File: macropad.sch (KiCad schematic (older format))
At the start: 13 parts

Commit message: added some wires
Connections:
- net labels added: COL0, COL1, GND, ROW0, ROW1, ROW2
- wire segments 0 -> 18
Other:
- moved on the sheet: D?, SW?
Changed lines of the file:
@@
 L Device:Rotary_Encoder_Switch SW?
 U 1 1 5D79E7D6
-P 3600 4300
-F 0 "SW?" H 3600 4667 50  0000 C CNN
-F 1 "Rotary_Encoder_Switch" H 3600 4576 50  0000 C CNN
-F 2 "" H 3450 4460 50  0001 C CNN
-F 3 "~" H 3600 4560 50  0001 C CNN
-	1    3600 4300
+P 3600 4350
+F 0 "SW?" H 3600 4717 50  0000 C CNN
+F 1 "Rotary_Encoder_Switch" H 3600 4626 50  0000 C CNN
+F 2 "" H 3450 4510 50  0001 C CNN
+F 3 "~" H 3600 4610 50  0001 C CNN
+	1    3600 4350
 	1    0    0    -1
 $EndComp
@@
 L Device:D_ALT D?
 U 1 1 5D79F668
-P 3900 4550
-F 0 "D?" V 3946 4471 50  0000 R CNN
-F 1 "D_ALT" V 3855 4471 50  0000 R CNN
-F 2 "" H 3900 4550 50  0001 C CNN
-F 3 "~" H 3900 4550 50  0001 C CNN
-	1    3900 4550
+P 3900 4600
+F 0 "D?" V 3946 4521 50  0000 R CNN
+F 1 "D_ALT" V 3855 4521 50  0000 R CNN
+F 2 "" H 3900 4600 50  0001 C CNN
+F 3 "~" H 3900 4600 50  0001 C CNN
+	1    3900 4600
 	0    -1   -1   0
 $EndComp
@@
 	0    -1   -1   0
 $EndComp
+Wire Wire Line
+	3950 2100 4300 2100
+Wire Wire Line
+	4300 2100 4300 3100
+Wire Wire Line
+	4300 3100 3900 3100
+Wire Wire Line
+	3900 4250 4300 4250
+Wire Wire Line
+	4300 4250 4300 3100
+Connection ~ 4300 3100
+Wire Wire Line
+	4300 2100 4300 1600
+Connection ~ 4300 2100
+Text GLabel 4300 1550 1    50   Input ~ 0
+COL0
+Text GLabel 5900 1550 1    50   Input ~ 0
+COL1
+Wire Wire Line
+	5900 1550 5900 2100
+Wire Wire Line
+	5900 2100 5650 2100
+Wire Wire Line
+	5900 2100 5900 3100
+Wire Wire Line
+	5900 3100 5650 3100
+Connection ~ 5900 2100
+Wire Wire Line
+	5900 3100 5900 4250
+Wire Wire Line
+	5900 4250 5650 4250
+Connection ~ 5900 3100
+Wire Wire Line
+	5650 2600 3950 2600
+Connection ~ 3950 2600
+Wire Wire Line
+	3950 2600 2800 2600
+Wire Wire Line
+	5650 3600 3900 3600
+Connection ~ 3900 3600
+Wire Wire Line
+	3900 3600 2800 3600
+Wire Wire Line
+	5650 4750 3900 4750
+Connection ~ 3900 4750
+Wire Wire Line
+	3900 4750 2800 4750
+Text GLabel 2800 2600 0    50   Input ~ 0
+ROW0
+Text GLabel 2800 3600 0    50   Input ~ 0
+ROW1
+Text GLabel 2800 4750 0    50   Input ~ 0
+ROW2
+Text GLabel 3350 2200 0    50   Input ~ 0
+GND
+Text GLabel 3300 3200 0    50   Input ~ 0
+GND
+Text GLabel 3300 4350 0    50   Input ~ 0
+GND
+Text GLabel 5050 2200 0    50   Input ~ 0
+GND
+Text GLabel 5050 3200 0    50   Input ~ 0
+GND
+Text GLabel 5050 4350 0    50   Input ~ 0
+GND
+Text GLabel 7100 2200 0    50   Input ~ 0
+GND
+Text GLabel 7100 2600 0    50   Input ~ 0
+ROW0
+Text GLabel 7100 2700 0    50   Input ~ 0
+ROW1
+Text GLabel 7100 2800 0    50   Input ~ 0
+ROW2
+Text GLabel 7100 2900 0    50   Input ~ 0
+COL0
+Text GLabel 7100 3000 0    50   Input ~ 0
+COL1
 $EndSCHEMATC

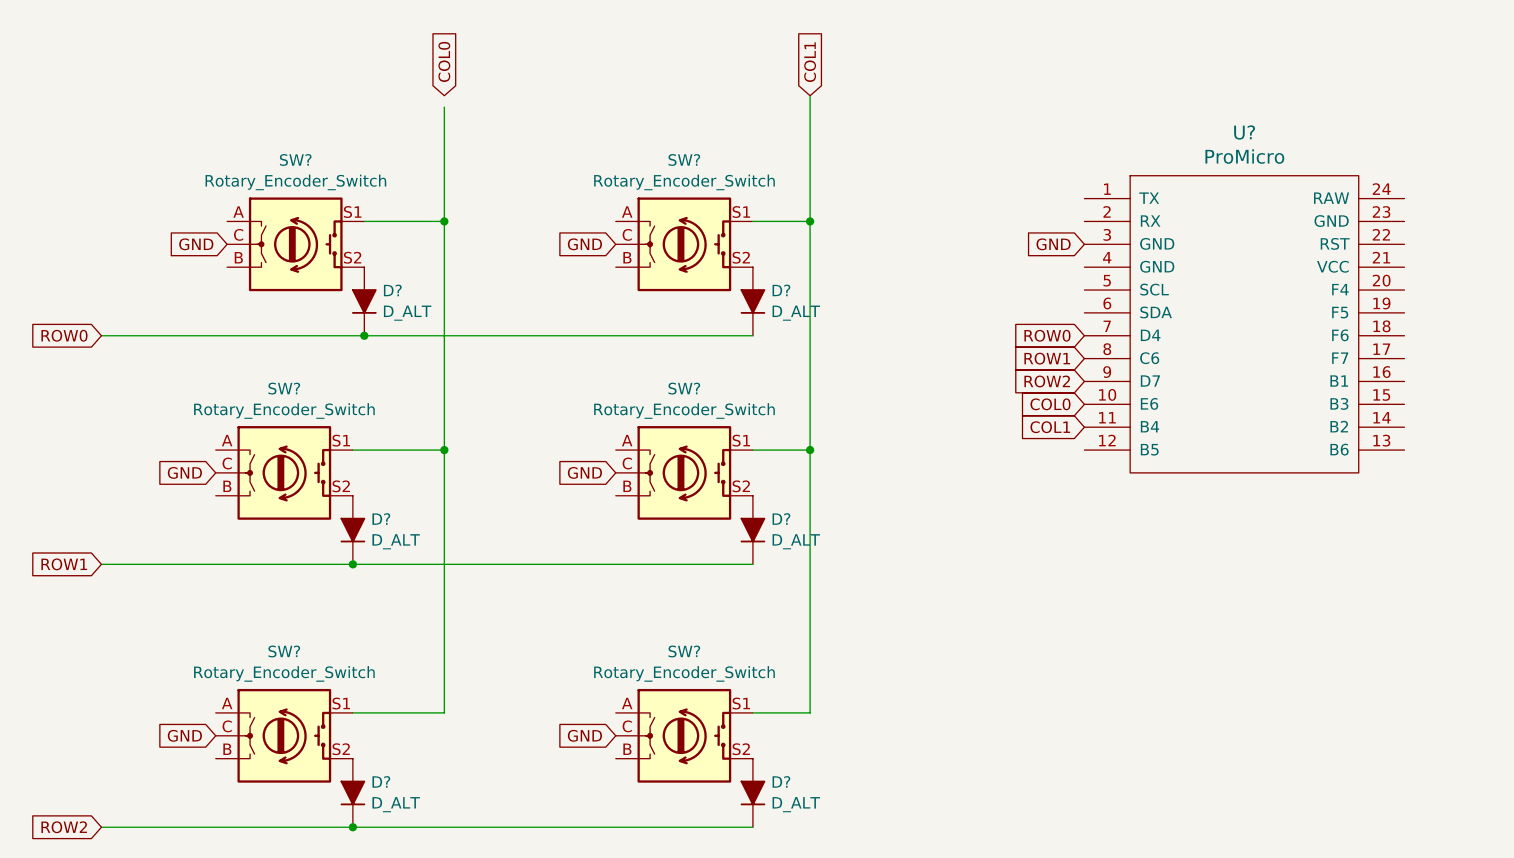
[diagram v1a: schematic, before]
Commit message: finished wiring and assigned footprints
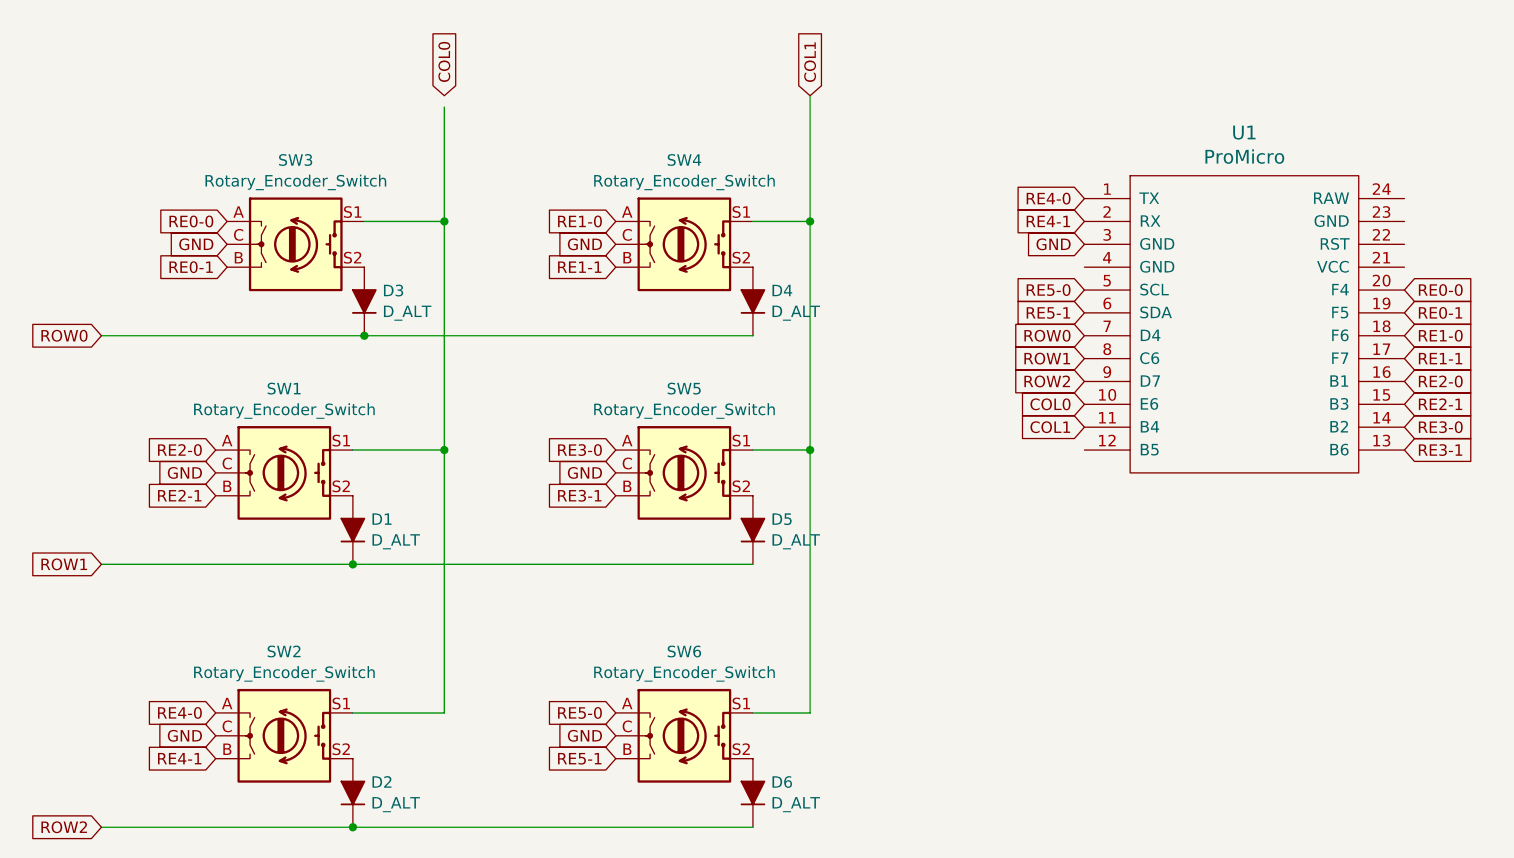
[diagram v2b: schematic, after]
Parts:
- D1, D2, D3, D4, D5, D6: renamed from D?; footprint (none) -> Keebio-Parts:Diode
- SW1, SW2, SW3, SW4, SW5, SW6: renamed from SW?; footprint (none) -> Keebio-Parts:RotaryEncoder_Alps_EC11E-Switch_Vertical_H20mm
- U1: renamed from U?; footprint (none) -> promicro:ProMicro
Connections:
- net labels added: RE0-0, RE0-1, RE1-0, RE1-1, RE2-0, RE2-1, RE3-0, RE3-1, RE4-0, RE4-1, RE5-0, RE5-1
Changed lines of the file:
@@
 EESchema Schematic File Version 4
-EELAYER 29 0
+LIBS:macropad-cache
+EELAYER 30 0
 EELAYER END
 $Descr A4 11693 8268
@@
 $EndDescr
 $Comp
-L promicro:ProMicro U?
+L promicro:ProMicro U1
 U 1 1 5D79AA52
 P 7800 2750
-F 0 "U?" H 7800 3787 60  0000 C CNN
+F 0 "U1" H 7800 3787 60  0000 C CNN
 F 1 "ProMicro" H 7800 3681 60  0000 C CNN
-F 2 "" H 7900 1700 60  0000 C CNN
+F 2 "promicro:ProMicro" H 7900 1700 60  0001 C CNN
 F 3 "" H 7900 1700 60  0000 C CNN
 	1    7800 2750
@@
 $EndComp
 $Comp
-L Device:Rotary_Encoder_Switch SW?
+L Device:Rotary_Encoder_Switch SW3
 U 1 1 5D79BB68
 P 3650 2200
-F 0 "SW?" H 3650 2567 50  0000 C CNN
+F 0 "SW3" H 3650 2567 50  0000 C CNN
 F 1 "Rotary_Encoder_Switch" H 3650 2476 50  0000 C CNN
-F 2 "" H 3500 2360 50  0001 C CNN
+F 2 "Keebio-Parts:RotaryEncoder_Alps_EC11E-Switch_Vertical_H20mm" H 3500 2360 50  0001 C CNN
 F 3 "~" H 3650 2460 50  0001 C CNN
 	1    3650 2200
@@
 $EndComp
 $Comp
-L Device:Rotary_Encoder_Switch SW?
+L Device:Rotary_Encoder_Switch SW1
 U 1 1 5D79D5D3
 P 3600 3200
-F 0 "SW?" H 3600 3567 50  0000 C CNN
+F 0 "SW1" H 3600 3567 50  0000 C CNN
 F 1 "Rotary_Encoder_Switch" H 3600 3476 50  0000 C CNN
-F 2 "" H 3450 3360 50  0001 C CNN
+F 2 "Keebio-Parts:RotaryEncoder_Alps_EC11E-Switch_Vertical_H20mm" H 3450 3360 50  0001 C CNN
 F 3 "~" H 3600 3460 50  0001 C CNN
 	1    3600 3200
@@
 $EndComp
 $Comp
-L Device:Rotary_Encoder_Switch SW?
+L Device:Rotary_Encoder_Switch SW2
 U 1 1 5D79E7D6
 P 3600 4350
-F 0 "SW?" H 3600 4717 50  0000 C CNN
+F 0 "SW2" H 3600 4717 50  0000 C CNN
 F 1 "Rotary_Encoder_Switch" H 3600 4626 50  0000 C CNN
-F 2 "" H 3450 4510 50  0001 C CNN
+F 2 "Keebio-Parts:RotaryEncoder_Alps_EC11E-Switch_Vertical_H20mm" H 3450 4510 50  0001 C CNN
 F 3 "~" H 3600 4610 50  0001 C CNN
 	1    3600 4350
@@
 $EndComp
 $Comp
-L Device:Rotary_Encoder_Switch SW?
+L Device:Rotary_Encoder_Switch SW4
 U 1 1 5D79FC8A
 P 5350 2200
-F 0 "SW?" H 5350 2567 50  0000 C CNN
+F 0 "SW4" H 5350 2567 50  0000 C CNN
 F 1 "Rotary_Encoder_Switch" H 5350 2476 50  0000 C CNN
-F 2 "" H 5200 2360 50  0001 C CNN
+F 2 "Keebio-Parts:RotaryEncoder_Alps_EC11E-Switch_Vertical_H20mm" H 5200 2360 50  0001 C CNN
 F 3 "~" H 5350 2460 50  0001 C CNN
 	1    5350 2200
@@
 $EndComp
 $Comp
-L Device:Rotary_Encoder_Switch SW?
+L Device:Rotary_Encoder_Switch SW5
 U 1 1 5D7A0733
 P 5350 3200
-F 0 "SW?" H 5350 3567 50  0000 C CNN
+F 0 "SW5" H 5350 3567 50  0000 C CNN
 F 1 "Rotary_Encoder_Switch" H 5350 3476 50  0000 C CNN
-F 2 "" H 5200 3360 50  0001 C CNN
+F 2 "Keebio-Parts:RotaryEncoder_Alps_EC11E-Switch_Vertical_H20mm" H 5200 3360 50  0001 C CNN
 F 3 "~" H 5350 3460 50  0001 C CNN
 	1    5350 3200
@@
 $EndComp
 $Comp
-L Device:Rotary_Encoder_Switch SW?
+L Device:Rotary_Encoder_Switch SW6
 U 1 1 5D7A1ADE
 P 5350 4350
-F 0 "SW?" H 5350 4717 50  0000 C CNN
+F 0 "SW6" H 5350 4717 50  0000 C CNN
 F 1 "Rotary_Encoder_Switch" H 5350 4626 50  0000 C CNN
-F 2 "" H 5200 4510 50  0001 C CNN
+F 2 "Keebio-Parts:RotaryEncoder_Alps_EC11E-Switch_Vertical_H20mm" H 5200 4510 50  0001 C CNN
 F 3 "~" H 5350 4610 50  0001 C CNN
 	1    5350 4350
@@
 $EndComp
 $Comp
-L Device:D_ALT D?
+L Device:D_ALT D3
 U 1 1 5D79D8B8
 P 3950 2450
-F 0 "D?" V 3996 2371 50  0000 R CNN
+F 0 "D3" V 3996 2371 50  0000 R CNN
 F 1 "D_ALT" V 3905 2371 50  0000 R CNN
-F 2 "" H 3950 2450 50  0001 C CNN
+F 2 "Keebio-Parts:Diode" H 3950 2450 50  0001 C CNN
 F 3 "~" H 3950 2450 50  0001 C CNN
 	1    3950 2450
@@
 $EndComp
 $Comp
-L Device:D_ALT D?
+L Device:D_ALT D1
 U 1 1 5D79E837
 P 3900 3450
-F 0 "D?" V 3946 3371 50  0000 R CNN
+F 0 "D1" V 3946 3371 50  0000 R CNN
 F 1 "D_ALT" V 3855 3371 50  0000 R CNN
-F 2 "" H 3900 3450 50  0001 C CNN
+F 2 "Keebio-Parts:Diode" H 3900 3450 50  0001 C CNN
 F 3 "~" H 3900 3450 50  0001 C CNN
 	1    3900 3450
@@
 $EndComp
 $Comp
-L Device:D_ALT D?
+L Device:D_ALT D2
 U 1 1 5D79F668
 P 3900 4600
-F 0 "D?" V 3946 4521 50  0000 R CNN
+F 0 "D2" V 3946 4521 50  0000 R CNN
 F 1 "D_ALT" V 3855 4521 50  0000 R CNN
-F 2 "" H 3900 4600 50  0001 C CNN
+F 2 "Keebio-Parts:Diode" H 3900 4600 50  0001 C CNN
 F 3 "~" H 3900 4600 50  0001 C CNN
 	1    3900 4600
@@
 $EndComp
 $Comp
-L Device:D_ALT D?
+L Device:D_ALT D4
 U 1 1 5D79FBB8
 P 5650 2450
-F 0 "D?" V 5696 2371 50  0000 R CNN
+F 0 "D4" V 5696 2371 50  0000 R CNN
 F 1 "D_ALT" V 5605 2371 50  0000 R CNN
-F 2 "" H 5650 2450 50  0001 C CNN
+F 2 "Keebio-Parts:Diode" H 5650 2450 50  0001 C CNN
 F 3 "~" H 5650 2450 50  0001 C CNN
 	1    5650 2450
@@
 $EndComp
 $Comp
-L Device:D_ALT D?
+L Device:D_ALT D5
 U 1 1 5D7A0234
 P 5650 3450
-F 0 "D?" V 5696 3371 50  0000 R CNN
+F 0 "D5" V 5696 3371 50  0000 R CNN
 F 1 "D_ALT" V 5605 3371 50  0000 R CNN
-F 2 "" H 5650 3450 50  0001 C CNN
+F 2 "Keebio-Parts:Diode" H 5650 3450 50  0001 C CNN
 F 3 "~" H 5650 3450 50  0001 C CNN
 	1    5650 3450
@@
 $EndComp
 $Comp
-L Device:D_ALT D?
+L Device:D_ALT D6
 U 1 1 5D7A05C2
 P 5650 4600
-F 0 "D?" V 5696 4521 50  0000 R CNN
+F 0 "D6" V 5696 4521 50  0000 R CNN
 F 1 "D_ALT" V 5605 4521 50  0000 R CNN
-F 2 "" H 5650 4600 50  0001 C CNN
+F 2 "Keebio-Parts:Diode" H 5650 4600 50  0001 C CNN
 F 3 "~" H 5650 4600 50  0001 C CNN
 	1    5650 4600
@@
 Text GLabel 7100 3000 0    50   Input ~ 0
 COL1
+Text GLabel 3350 2100 0    50   Input ~ 0
+RE0-0
+Text GLabel 3350 2300 0    50   Input ~ 0
+RE0-1
+Text GLabel 5050 2100 0    50   Input ~ 0
+RE1-0
+Text GLabel 5050 2300 0    50   Input ~ 0
+RE1-1
+Text GLabel 3300 3100 0    50   Input ~ 0
+RE2-0
+Text GLabel 3300 3300 0    50   Input ~ 0
+RE2-1
+Text GLabel 5050 3100 0    50   Input ~ 0
+RE3-0
+Text GLabel 5050 3300 0    50   Input ~ 0
+RE3-1
+Text GLabel 3300 4250 0    50   Input ~ 0
+RE4-0
+Text GLabel 3300 4450 0    50   Input ~ 0
+RE4-1
+Text GLabel 5050 4250 0    50   Input ~ 0
+RE5-0
+Text GLabel 5050 4450 0    50   Input ~ 0
+RE5-1
+Text GLabel 8500 2400 2    50   Input ~ 0
+RE0-0
+Text GLabel 8500 2500 2    50   Input ~ 0
+RE0-1
+Text GLabel 8500 2600 2    50   Input ~ 0
+RE1-0
+Text GLabel 8500 2700 2    50   Input ~ 0
+RE1-1
+Text GLabel 8500 2800 2    50   Input ~ 0
+RE2-0
+Text GLabel 8500 2900 2    50   Input ~ 0
+RE2-1
+Text GLabel 8500 3000 2    50   Input ~ 0
+RE3-0
+Text GLabel 8500 3100 2    50   Input ~ 0
+RE3-1
+Text GLabel 7100 2000 0    50   Input ~ 0
+RE4-0
+Text GLabel 7100 2100 0    50   Input ~ 0
+RE4-1
+Text GLabel 7100 2400 0    50   Input ~ 0
+RE5-0
+Text GLabel 7100 2500 0    50   Input ~ 0
+RE5-1
 $EndSCHEMATC

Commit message: moved to 70mm circle, just before routing
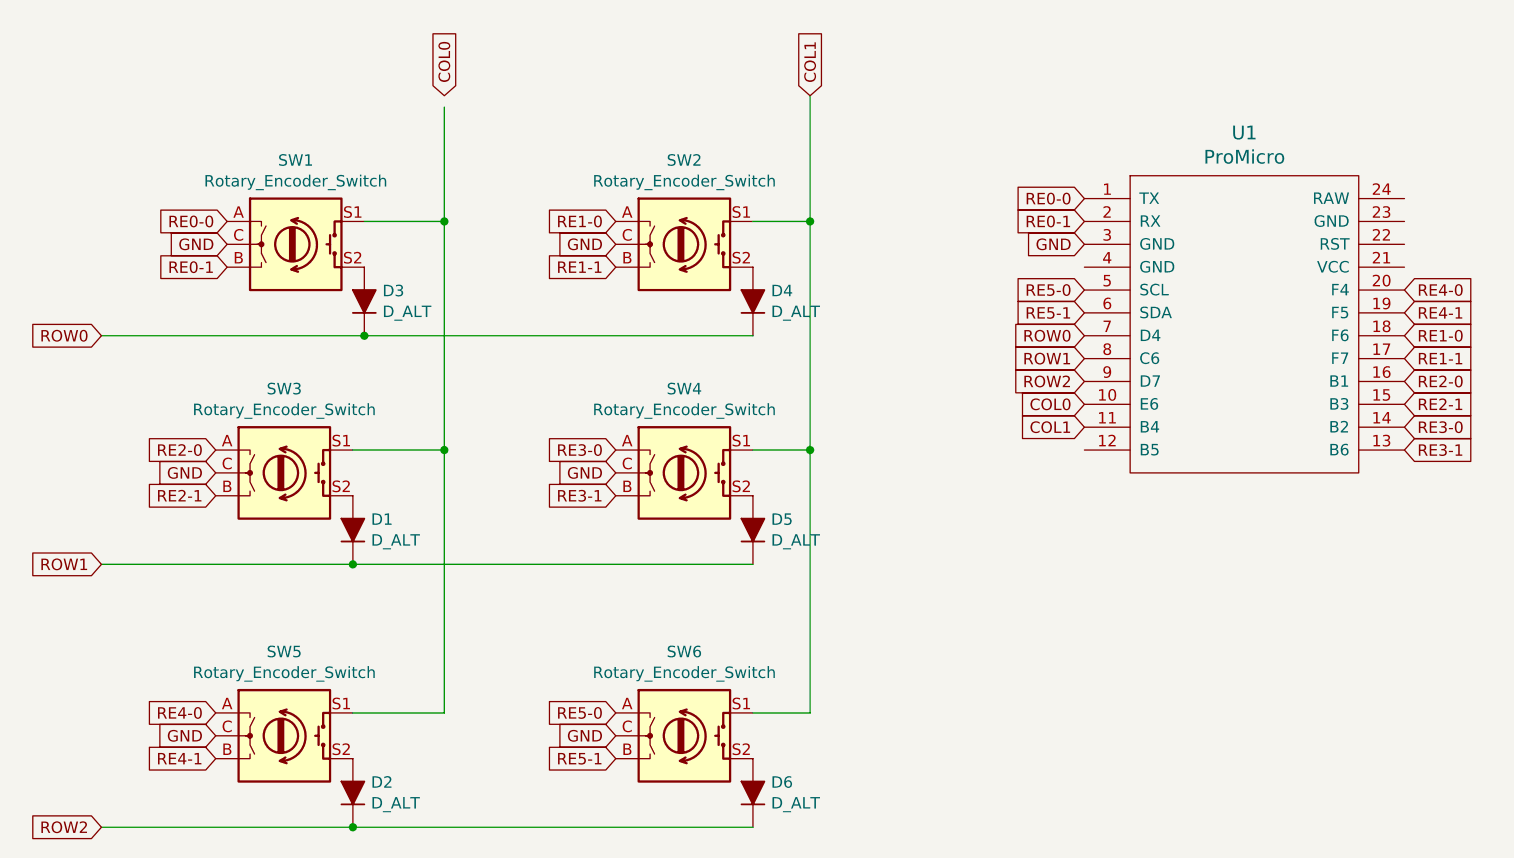
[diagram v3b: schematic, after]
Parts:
- renumbered SW3 to SW1, SW4 to SW2, SW1 to SW3, SW5 to SW4, SW2 to SW5
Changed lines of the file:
@@
 $EndComp
 $Comp
-L Device:Rotary_Encoder_Switch SW3
+L Device:Rotary_Encoder_Switch SW1
 U 1 1 5D79BB68
 P 3650 2200
-F 0 "SW3" H 3650 2567 50  0000 C CNN
+F 0 "SW1" H 3650 2567 50  0000 C CNN
 F 1 "Rotary_Encoder_Switch" H 3650 2476 50  0000 C CNN
 F 2 "Keebio-Parts:RotaryEncoder_Alps_EC11E-Switch_Vertical_H20mm" H 3500 2360 50  0001 C CNN
@@
 $EndComp
 $Comp
-L Device:Rotary_Encoder_Switch SW1
+L Device:Rotary_Encoder_Switch SW3
 U 1 1 5D79D5D3
 P 3600 3200
-F 0 "SW1" H 3600 3567 50  0000 C CNN
+F 0 "SW3" H 3600 3567 50  0000 C CNN
 F 1 "Rotary_Encoder_Switch" H 3600 3476 50  0000 C CNN
 F 2 "Keebio-Parts:RotaryEncoder_Alps_EC11E-Switch_Vertical_H20mm" H 3450 3360 50  0001 C CNN
@@
 $EndComp
 $Comp
-L Device:Rotary_Encoder_Switch SW2
+L Device:Rotary_Encoder_Switch SW5
 U 1 1 5D79E7D6
 P 3600 4350
-F 0 "SW2" H 3600 4717 50  0000 C CNN
+F 0 "SW5" H 3600 4717 50  0000 C CNN
 F 1 "Rotary_Encoder_Switch" H 3600 4626 50  0000 C CNN
 F 2 "Keebio-Parts:RotaryEncoder_Alps_EC11E-Switch_Vertical_H20mm" H 3450 4510 50  0001 C CNN
@@
 $EndComp
 $Comp
-L Device:Rotary_Encoder_Switch SW4
+L Device:Rotary_Encoder_Switch SW2
 U 1 1 5D79FC8A
 P 5350 2200
-F 0 "SW4" H 5350 2567 50  0000 C CNN
+F 0 "SW2" H 5350 2567 50  0000 C CNN
 F 1 "Rotary_Encoder_Switch" H 5350 2476 50  0000 C CNN
 F 2 "Keebio-Parts:RotaryEncoder_Alps_EC11E-Switch_Vertical_H20mm" H 5200 2360 50  0001 C CNN
@@
 $EndComp
 $Comp
-L Device:Rotary_Encoder_Switch SW5
+L Device:Rotary_Encoder_Switch SW4
 U 1 1 5D7A0733
 P 5350 3200
-F 0 "SW5" H 5350 3567 50  0000 C CNN
+F 0 "SW4" H 5350 3567 50  0000 C CNN
 F 1 "Rotary_Encoder_Switch" H 5350 3476 50  0000 C CNN
 F 2 "Keebio-Parts:RotaryEncoder_Alps_EC11E-Switch_Vertical_H20mm" H 5200 3360 50  0001 C CNN
@@
 Text GLabel 5050 4450 0    50   Input ~ 0
 RE5-1
-Text GLabel 8500 2400 2    50   Input ~ 0
+Text GLabel 7100 2000 0    50   Input ~ 0
 RE0-0
-Text GLabel 8500 2500 2    50   Input ~ 0
+Text GLabel 7100 2100 0    50   Input ~ 0
 RE0-1
 Text GLabel 8500 2600 2    50   Input ~ 0
@@
 Text GLabel 8500 3100 2    50   Input ~ 0
 RE3-1
-Text GLabel 7100 2000 0    50   Input ~ 0
+Text GLabel 8500 2400 2    50   Input ~ 0
 RE4-0
-Text GLabel 7100 2100 0    50   Input ~ 0
+Text GLabel 8500 2500 2    50   Input ~ 0
 RE4-1
 Text GLabel 7100 2400 0    50   Input ~ 0
